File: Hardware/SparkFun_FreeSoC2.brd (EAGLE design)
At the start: 116.8 x 53.3 mm, 108 parts, among them U1 CY8C5888AXI-LP096, U2 MIC5219 5V, U3 MIC5219 3.3V, U4 2A/20V, U7 CY8C5868LTI-LP039, Y1 32.768kHz

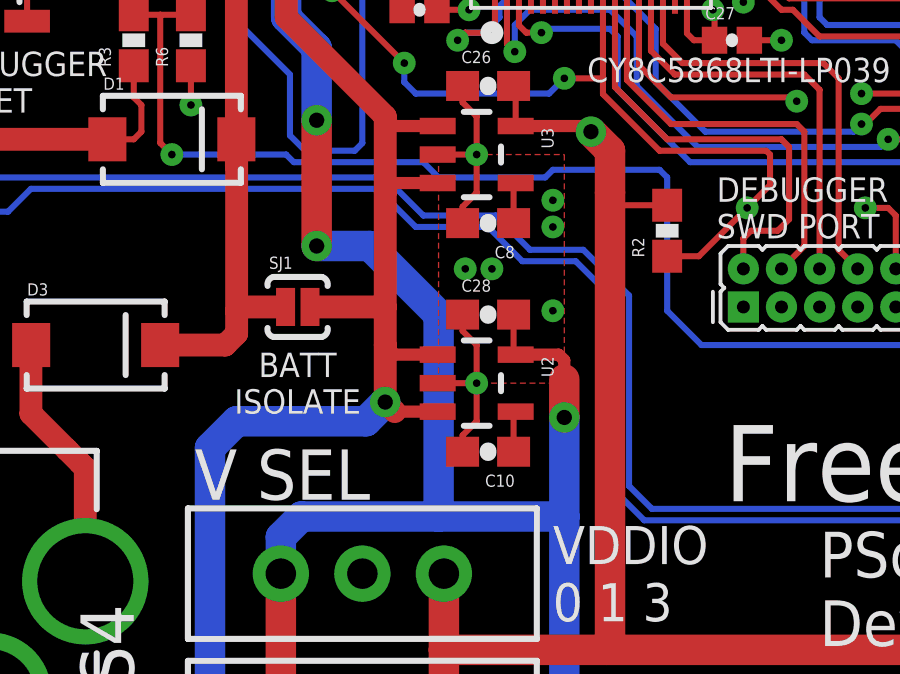
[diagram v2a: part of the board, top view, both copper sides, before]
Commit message: Changes from user feedback and experience
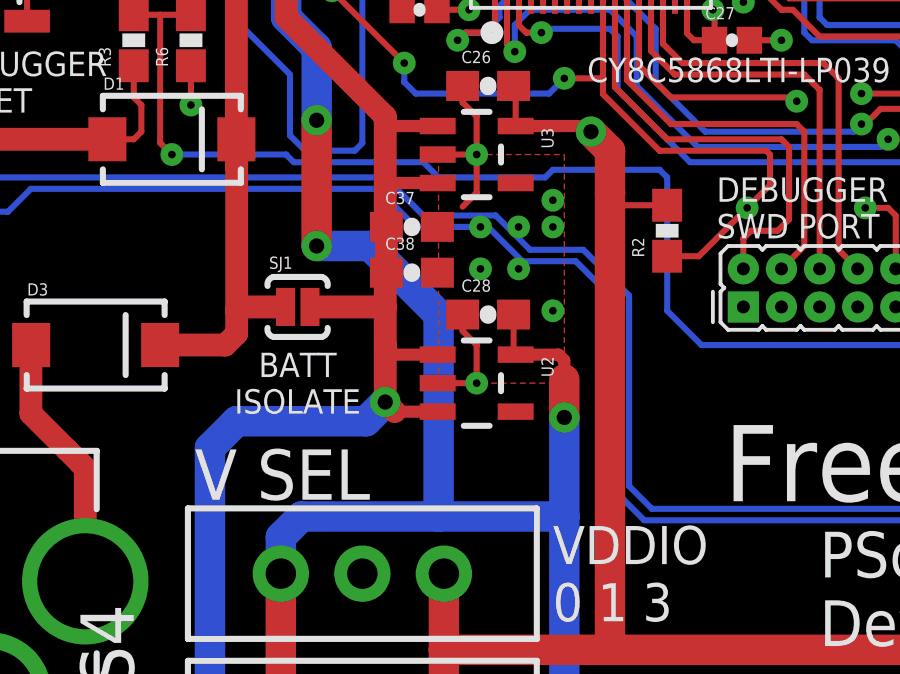
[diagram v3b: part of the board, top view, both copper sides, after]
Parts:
- removed C10, C8: 470pF, SparkFun-Capacitors:0603-CAP
- added C37: 1.0uF, SparkFun-Capacitors:0603-CAP
- added C38: 0.1uF, SparkFun-Capacitors:0603-CAP
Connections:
- removed net N$1: C8.1, U3.4
- net GND: now also C37.2, C38.2; no longer C10.2, C8.2
- net N$2: no longer C10.1
- net V_IN: now also C37.1, C38.1
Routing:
- net GND: track 130.6 -> 127.6 mm, vias 46 -> 48
- net N$1: track 1.36 -> 0.00 mm
- net N$2: track 1.36 -> 0.10 mm
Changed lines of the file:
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@@
 <layers>
 <layer number="1" name="Top" color="4" fill="1" visible="yes" active="yes"/>
-<layer number="2" name="Route2" color="1" fill="3" visible="no" active="yes"/>
-<layer number="15" name="Route15" color="4" fill="6" visible="no" active="yes"/>
+<layer number="2" name="Route2" color="1" fill="3" visible="yes" active="yes"/>
+<layer number="15" name="Route15" color="4" fill="6" visible="yes" active="yes"/>
 <layer number="16" name="Bottom" color="1" fill="1" visible="yes" active="yes"/>
 <layer number="17" name="Pads" color="2" fill="1" visible="yes" active="yes"/>
@@
 <layer number="23" name="tOrigins" color="15" fill="1" visible="yes" active="yes"/>
 <layer number="24" name="bOrigins" color="15" fill="1" visible="yes" active="yes"/>
-<layer number="25" name="tNames" color="7" fill="1" visible="no" active="yes"/>
-<layer number="26" name="bNames" color="7" fill="1" visible="no" active="yes"/>
-<layer number="27" name="tValues" color="7" fill="1" visible="no" active="yes"/>
-<layer number="28" name="bValues" color="7" fill="1" visible="no" active="yes"/>
-<layer number="29" name="tStop" color="7" fill="3" visible="no" active="yes"/>
-<layer number="30" name="bStop" color="7" fill="6" visible="no" active="yes"/>
-<layer number="31" name="tCream" color="7" fill="4" visible="no" active="yes"/>
-<layer number="32" name="bCream" color="7" fill="5" visible="no" active="yes"/>
-<layer number="39" name="tKeepout" color="4" fill="11" visible="no" active="yes"/>
-<layer number="40" name="bKeepout" color="1" fill="11" visible="no" active="yes"/>
-<layer number="41" name="tRestrict" color="4" fill="10" visible="no" active="yes"/>
-<layer number="42" name="bRestrict" color="1" fill="10" visible="no" active="yes"/>
-<layer number="43" name="vRestrict" color="2" fill="10" visible="no" active="yes"/>
-<layer number="44" name="Drills" color="7" fill="1" visible="no" active="yes"/>
+<layer number="25" name="tNames" color="7" fill="1" visible="yes" active="yes"/>
+<layer number="26" name="bNames" color="7" fill="1" visible="yes" active="yes"/>
+<layer number="27" name="tValues" color="7" fill="1" visible="yes" active="yes"/>
+<layer number="28" name="bValues" color="7" fill="1" visible="yes" active="yes"/>
+<layer number="29" name="tStop" color="7" fill="3" visible="yes" active="yes"/>
+<layer number="30" name="bStop" color="7" fill="6" visible="yes" active="yes"/>
+<layer number="31" name="tCream" color="7" fill="4" visible="yes" active="yes"/>
+<layer number="32" name="bCream" color="7" fill="5" visible="yes" active="yes"/>
+<layer number="39" name="tKeepout" color="4" fill="11" visible="yes" active="yes"/>
+<layer number="40" name="bKeepout" color="1" fill="11" visible="yes" active="yes"/>
+<layer number="41" name="tRestrict" color="4" fill="10" visible="yes" active="yes"/>
+<layer number="42" name="bRestrict" color="1" fill="10" visible="yes" active="yes"/>
+<layer number="43" name="vRestrict" color="2" fill="10" visible="yes" active="yes"/>
+<layer number="44" name="Drills" color="7" fill="1" visible="yes" active="yes"/>
 <layer number="45" name="Holes" color="7" fill="1" visible="yes" active="yes"/>
-<layer number="46" name="Milling" color="3" fill="1" visible="no" active="yes"/>
-<layer number="47" name="Measures" color="7" fill="1" visible="no" active="yes"/>
+<layer number="46" name="Milling" color="3" fill="1" visible="yes" active="yes"/>
+<layer number="47" name="Measures" color="7" fill="1" visible="yes" active="yes"/>
 <layer number="51" name="tDocu" color="6" fill="1" visible="yes" active="yes"/>
 <layer number="52" name="bDocu" color="7" fill="1" visible="no" active="no"/>
@@
 <attribute name="PROD_ID" value="VREG-09872" x="24.13" y="24.13" size="1.778" layer="27" font="vector" ratio="15" rot="R270" display="off"/>
 </element>
-<element name="C8" library="SparkFun-Capacitors" package="0603-CAP" value="470pF" x="24.511" y="21.844" rot="R180">
-<attribute name="PROD_ID" value="CAP-07884" x="24.511" y="21.844" size="1.778" layer="27" font="vector" ratio="15" rot="R180" display="off"/>
-</element>
-<element name="C10" library="SparkFun-Capacitors" package="0603-CAP" value="470pF" x="24.511" y="14.224" rot="R180">
-<attribute name="PROD_ID" value="CAP-07884" x="24.511" y="14.224" size="1.778" layer="27" font="vector" ratio="15" rot="R180" display="off"/>
-</element>
 <element name="S3" library="SparkFun-Electromechanical" package="SWITCH-SPDT_LOCK.007S" value="SPDT" x="20.32" y="5.08" rot="R90">
 <attribute name="PROD_ID" value="SWCH-08261" x="20.32" y="5.08" size="1.778" layer="27" rot="R90" display="off"/>
@@
 <element name="C18" library="SparkFun-Capacitors" package="CAP-PTH-SMALL" value="" x="80.645" y="22.86" rot="R90"/>
 <element name="C24" library="SparkFun-Capacitors" package="CAP-PTH-SMALL" value="" x="75.565" y="22.86" rot="R90"/>
+<element name="C37" library="SparkFun-Capacitors" package="0603-CAP" value="1.0uF" x="21.971" y="21.717">
+<attribute name="PROD_ID" value="CAP-00868" x="21.971" y="21.717" size="1.27" layer="27" font="vector" ratio="15" display="off"/>
+</element>
+<element name="C38" library="SparkFun-Capacitors" package="0603-CAP" value="0.1uF" x="21.971" y="20.193">
+<attribute name="PROD_ID" value="CAP-00810" x="21.971" y="20.193" size="1.27" layer="27" font="vector" ratio="15" display="off"/>
+</element>
 </elements>
 <signals>
@@
 <contactref element="U2" pad="2"/>
 <contactref element="U3" pad="2"/>
-<contactref element="C8" pad="2"/>
-<contactref element="C10" pad="2"/>
 <contactref element="C16" pad="2"/>
 <contactref element="U7" pad="8"/>
@@
 <wire x1="24.13" y1="25.4" x2="23.661" y2="25.869" width="0.2032" layer="1"/>
 <wire x1="23.661" y1="26.416" x2="23.661" y2="25.869" width="0.2032" layer="1"/>
-<wire x1="23.661" y1="21.844" x2="23.661" y2="22.391" width="0.2032" layer="1"/>
 <wire x1="23.661" y1="22.391" x2="24.13" y2="22.86" width="0.2032" layer="1"/>
 <wire x1="24.13" y1="22.86" x2="24.13" y2="24.13" width="0.2032" layer="1"/>
@@
 <wire x1="23.661" y1="18.796" x2="23.661" y2="18.249" width="0.2032" layer="1"/>
 <wire x1="23.661" y1="18.249" x2="24.13" y2="17.78" width="0.2032" layer="1"/>
-<wire x1="23.661" y1="14.224" x2="23.661" y2="14.771" width="0.2032" layer="1"/>
-<wire x1="23.661" y1="14.771" x2="24.13" y2="15.24" width="0.2032" layer="1"/>
-<wire x1="24.13" y1="15.24" x2="24.13" y2="16.51" width="0.2032" layer="1"/>
 <wire x1="25.781" y1="33.782" x2="27.178" y2="33.782" width="0.2032" layer="1"/>
 <wire x1="27.178" y1="33.782" x2="27.94" y2="33.02" width="0.2032" layer="1"/>
@@
 <via x="26.67" y="22.606" extent="1-16" drill="0.254"/>
 <via x="26.67" y="18.923" extent="1-16" drill="0.254"/>
-<via x="24.638" y="20.32" extent="1-16" drill="0.254"/>
-<via x="23.749" y="20.32" extent="1-16" drill="0.254"/>
+<via x="24.257" y="21.717" extent="1-16" drill="0.254"/>
+<via x="24.257" y="20.32" extent="1-16" drill="0.254"/>
 <contactref element="C13" pad="2"/>
 <contactref element="C15" pad="2"/>
@@
 <contactref element="C18" pad="2"/>
 <contactref element="C24" pad="2"/>
+<contactref element="C38" pad="2"/>
+<contactref element="C37" pad="2"/>
+<via x="25.527" y="21.717" extent="1-16" drill="0.254"/>
+<via x="25.527" y="20.32" extent="1-16" drill="0.254"/>
 </signal>
 <signal name="N$13">
@@
 <wire x1="17.78" y1="28.702" x2="21.082" y2="25.4" width="0.762" layer="1"/>
 <wire x1="21.082" y1="25.4" x2="21.082" y2="22.86" width="0.762" layer="1"/>
-<wire x1="21.082" y1="22.86" x2="21.082" y2="19.05" width="0.762" layer="1"/>
-<wire x1="21.082" y1="19.05" x2="21.082" y2="17.78" width="0.762" layer="1"/>
 <wire x1="18.5737" y1="19.05" x2="18.796" y2="19.05" width="0.4064" layer="1"/>
-<wire x1="18.796" y1="19.05" x2="21.082" y2="19.05" width="0.762" layer="1"/>
 <wire x1="22.8299" y1="17.46" x2="21.402" y2="17.46" width="0.4064" layer="1"/>
 <wire x1="21.402" y1="17.46" x2="21.082" y2="17.78" width="0.4064" layer="1"/>
@@
 <wire x1="17.762" y1="46.228" x2="16.383" y2="46.228" width="0.762" layer="1"/>
 <wire x1="16.071" y1="46.228" x2="16.383" y2="46.228" width="0.4064" layer="1"/>
+<contactref element="C37" pad="1"/>
+<contactref element="C38" pad="1"/>
+<wire x1="21.082" y1="22.86" x2="21.082" y2="21.756" width="0.762" layer="1"/>
+<wire x1="21.082" y1="21.756" x2="21.121" y2="21.717" width="0.762" layer="1"/>
+<wire x1="21.121" y1="21.717" x2="21.121" y2="20.193" width="0.762" layer="1"/>
+<wire x1="21.082" y1="17.78" x2="21.082" y2="19.05" width="0.762" layer="1"/>
+<wire x1="21.082" y1="19.05" x2="21.082" y2="20.154" width="0.762" layer="1"/>
+<wire x1="21.082" y1="20.154" x2="21.121" y2="20.193" width="0.762" layer="1"/>
+<wire x1="18.796" y1="19.05" x2="21.082" y2="19.05" width="0.762" layer="1"/>
 </signal>
 <signal name="PSOC_D+_BUS">
@@
 <wire x1="30.425" y1="39.569" x2="30.226" y2="39.37" width="0.2032" layer="1"/>
 </signal>
-<signal name="N$1">
-<contactref element="U3" pad="4"/>
-<contactref element="C8" pad="1"/>
-<wire x1="25.361" y1="21.844" x2="25.361" y2="23.1109" width="0.2032" layer="1"/>
-<wire x1="25.361" y1="23.1109" x2="25.4301" y2="23.18" width="0.2032" layer="1"/>
-</signal>
 <signal name="N$2">
 <contactref element="U2" pad="4"/>
-<contactref element="C10" pad="1"/>
-<wire x1="25.361" y1="14.224" x2="25.361" y2="15.4909" width="0.2032" layer="1"/>
 <wire x1="25.361" y1="15.4909" x2="25.4301" y2="15.56" width="0.2032" layer="1"/>
 </signal>
